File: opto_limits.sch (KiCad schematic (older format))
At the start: 18 parts, among them U1 LTV-847, U2 LTV-847

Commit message: Changed wrong GND for limit switches
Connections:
- net labels added: GND
- net labels removed: OPTO_GND
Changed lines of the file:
@@
 Connection ~ 9650 3300
 Wire Wire Line
-	3400 3450 3400 3400
-Wire Wire Line
-	8550 3450 8550 3400
-Wire Wire Line
 	3300 2800 3400 2800
 Wire Wire Line
@@
 	8550 3400 8550 3200
 Wire Wire Line
+	3400 3400 3400 3650
+Wire Wire Line
 	3550 2700 3300 2700
 Wire Wire Line
@@
 Wire Wire Line
 	4200 2250 4500 2250
+Wire Wire Line
+	8550 3400 8550 3700
 Wire Wire Line
 	9050 2250 9350 2250
@@
 Text GLabel 850  2250 1    50   Input ~ 0
 OPTO_5V
-Text GLabel 3400 3450 3    50   Input ~ 0
-OPTO_GND
 Text GLabel 6000 2250 1    50   Input ~ 0
 OPTO_5V
-Text GLabel 8550 3450 3    50   Input ~ 0
-OPTO_GND
 Text HLabel 2700 2800 0    50   Input ~ 0
 SW_XMIN
@@
 	1    0    0    -1
 $EndComp
+$Comp
+L power:GND #PWR010
+U 1 1 5E3FEA16
+P 3400 3650
+F 0 "#PWR010" H 3400 3400 50  0001 C CNN
+F 1 "GND" H 3405 3477 50  0000 C CNN
+F 2 "" H 3400 3650 50  0001 C CNN
+F 3 "" H 3400 3650 50  0001 C CNN
+	1    3400 3650
+	1    0    0    -1
+$EndComp
+$Comp
+L power:GND #PWR011
+U 1 1 5E3FFBB7
+P 8550 3700
+F 0 "#PWR011" H 8550 3450 50  0001 C CNN
+F 1 "GND" H 8555 3527 50  0000 C CNN
+F 2 "" H 8550 3700 50  0001 C CNN
+F 3 "" H 8550 3700 50  0001 C CNN
+	1    8550 3700
+	1    0    0    -1
+$EndComp

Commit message: Change mosfets and resistors to arrays
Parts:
- removed R29, R30, R31, R32, R33, R34, R35, R36: 220R, Resistor_SMD:R_1206_3216Metric_Pad1.42x1.75mm_HandSolder, symbol Device:R_US
- removed R37, R38, R39, R40, R41, R42, R43, R44: 4K7, Resistor_SMD:R_1206_3216Metric_Pad1.42x1.75mm_HandSolder, symbol Device:R_US
- added RN1: CAY17-472JALF, Kicad_extra_components:RESCAXS64P320X160X60-10N, symbol CAY17-103JALF:CAY17-103JALF
- added RN2: CAY17-221JALF, Kicad_extra_components:RESCAXS64P320X160X60-10N, symbol CAY17-103JALF:CAY17-103JALF
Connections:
- net labels added: Probe
- net labels removed: e
- wire segments 72 -> 75
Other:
- moved on the sheet: U1, U2

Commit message: More symbols fixed
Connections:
- net labels added: +3V3
- net labels removed: +3.3V
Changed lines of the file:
@@
 $Descr A4 11693 8268
 encoding utf-8
-Sheet 6 6
+Sheet 5 6
 Title ""
 Date "2020-02-12"
@@
 Extra_SW
 $Comp
-L power:+3.3V #PWR0122
-U 1 1 5E470105
+L power:+3V3 #PWR?
+U 1 1 5E47CFB2
 P 5200 2550
-F 0 "#PWR0122" H 5200 2400 50  0001 C CNN
-F 1 "+3.3V" H 5215 2723 50  0000 C CNN
+F 0 "#PWR?" H 5200 2400 50  0001 C CNN
+F 1 "+3V3" H 5215 2723 50  0000 C CNN
 F 2 "" H 5200 2550 50  0001 C CNN
 F 3 "" H 5200 2550 50  0001 C CNN
@@
 $EndComp
 $Comp
-L power:+3.3V #PWR023
-U 1 1 5E4A5430
+L power:+3V3 #PWR0105
+U 1 1 5E4719D1
 P 6050 1750
-F 0 "#PWR023" H 6050 1600 50  0001 C CNN
-F 1 "+3.3V" H 6065 1923 50  0000 C CNN
+F 0 "#PWR0105" H 6050 1600 50  0001 C CNN
+F 1 "+3V3" H 6065 1923 50  0000 C CNN
 F 2 "" H 6050 1750 50  0001 C CNN
 F 3 "" H 6050 1750 50  0001 C CNN

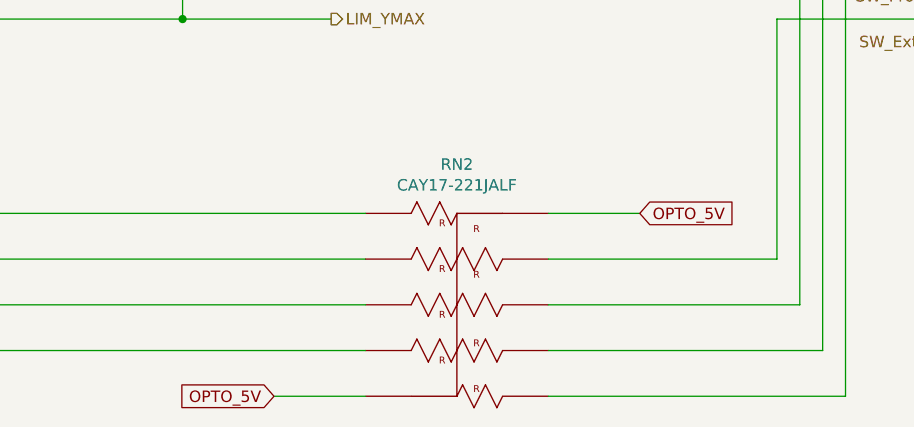
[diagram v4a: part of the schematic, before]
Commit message: Simplify the power options
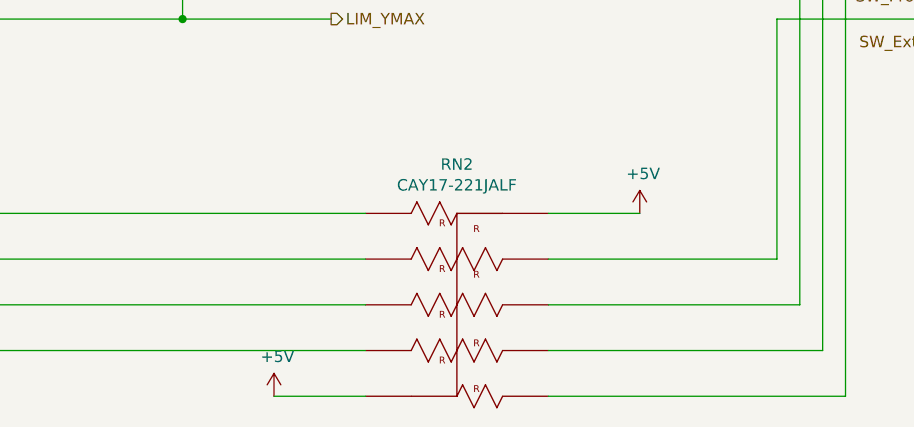
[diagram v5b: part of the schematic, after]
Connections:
- net OPTO_5V renamed +5V
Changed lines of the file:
@@
 $Descr A4 11693 8268
 encoding utf-8
-Sheet 5 6
+Sheet 6 6
 Title ""
 Date "2020-02-12"
@@
 Wire Wire Line
 	9600 3800 10250 3800
-Text GLabel 4850 6050 0    50   Input ~ 0
-OPTO_5V
-Text GLabel 6450 5250 2    50   Input ~ 0
-OPTO_5V
 Text HLabel 2650 3900 0    50   Input ~ 0
 SW_XMIN
@@
 Extra_SW
 $Comp
+L power:+5V #PWR?
+U 1 1 5E486E4C
+P 4850 6050
+F 0 "#PWR?" H 4850 5900 50  0001 C CNN
+F 1 "+5V" H 4865 6223 50  0000 C CNN
+F 2 "" H 4850 6050 50  0001 C CNN
+F 3 "" H 4850 6050 50  0001 C CNN
+	1    4850 6050
+	1    0    0    -1
+$EndComp
+$Comp
 L power:+3V3 #PWR?
 U 1 1 5E47CFB2
@@
 	1    0    0    -1
 $EndComp
+$Comp
+L power:+5V #PWR?
+U 1 1 5E488231
+P 6450 5250
+F 0 "#PWR?" H 6450 5100 50  0001 C CNN
+F 1 "+5V" H 6465 5423 50  0000 C CNN
+F 2 "" H 6450 5250 50  0001 C CNN
+F 3 "" H 6450 5250 50  0001 C CNN
+	1    6450 5250
+	1    0    0    -1
+$EndComp
